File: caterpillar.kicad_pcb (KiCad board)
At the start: 4 copper layers, 18.3 x 20.3 mm, 33 parts, among them J1 Conn_ARM_JTAG_SWD_10, J2 SM02B-SRSS-TB_LF__SN_, J3 Castellated_2PTH_P1.27mm, J4 Castellated_2PTH_P1.27mm, M2 *, U1 STBB1-APUR, U2 ASM330LHHTR, U3 DRV8212P, U4 ADP2503ACPZ-3.3-R7, U6 max5419leta+T

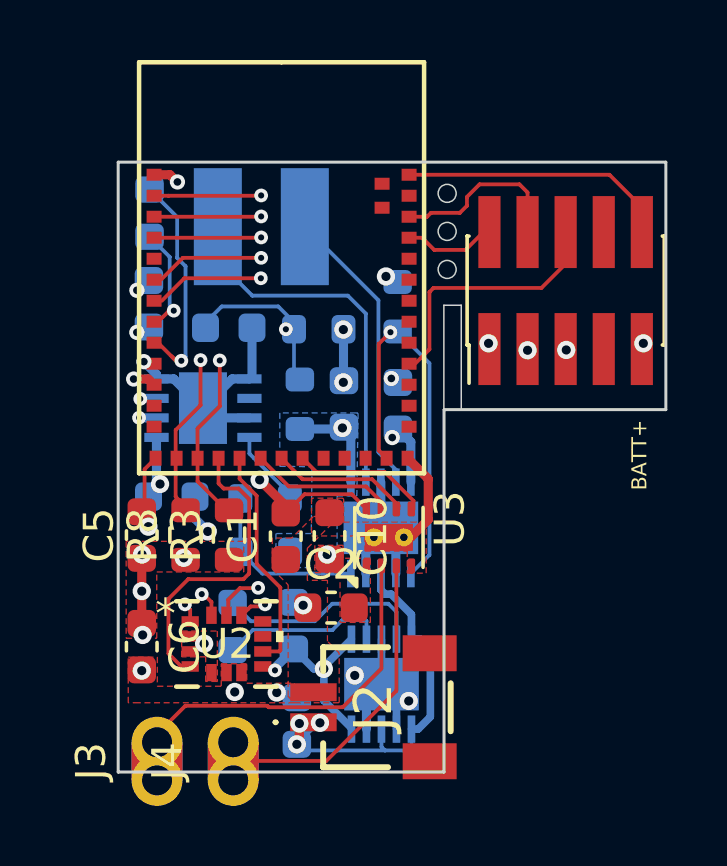
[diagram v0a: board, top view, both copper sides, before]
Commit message: all electrical issues fixed. Add as many vias as possible. connected nets on the same layer with polygon fills as much as possible. vias roughly realigned so looks much better
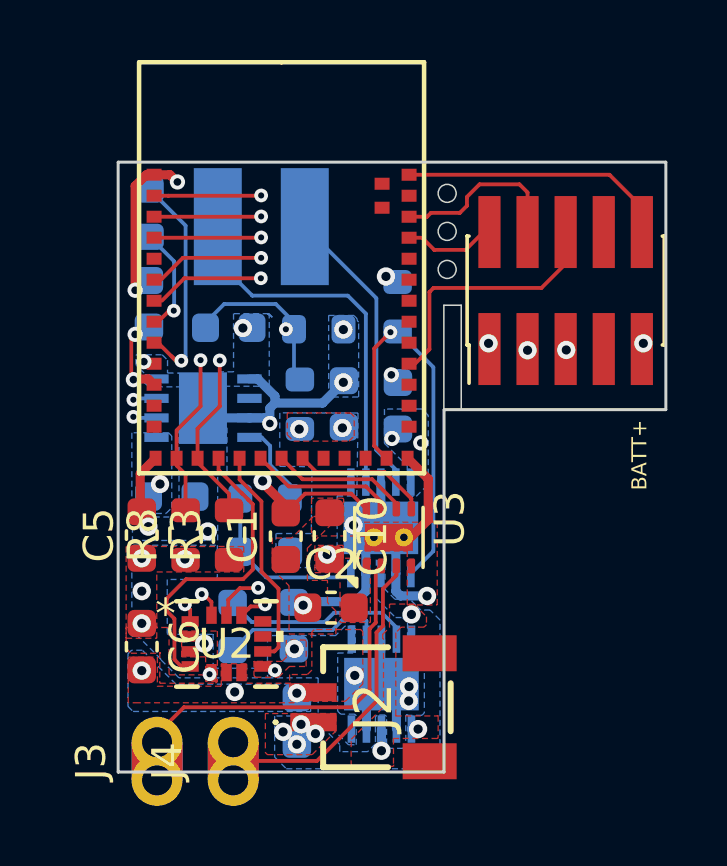
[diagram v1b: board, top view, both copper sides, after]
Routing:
- net +BATT: track 15.6 -> 1.89 mm, vias 4 -> 9
- net +3.3V: track 15.2 -> 7.11 mm, vias 12 -> 13
- net GND: track 26.8 -> 31.7 mm, vias 18 -> 23
- net VDC: track 3.42 -> 0.41 mm, vias 2 -> 3
- net /SCL: track 9.56 -> 10.5 mm
- net /CS: track 19.3 -> 20.3 mm
- net /SDA: track 8.97 -> 9.89 mm
- net /SCLK: track 18.7 -> 19.5 mm
- net /MISO: track 16.2 -> 16.7 mm
- net Net-(U4-SW1): track 6.98 -> 6.45 mm
- net /MOSI: track 16.9 -> 17.4 mm
- added copper zone on B.Cu, net +3.3V
- added copper zone on B.Cu, net +BATT
- added copper zone on F.Cu, net +BATT
- added copper zone on B.Cu, net GND

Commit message: thickened the power tracks of motor driver, added more vias for VDC output, moved VDC_sense away from the SW2
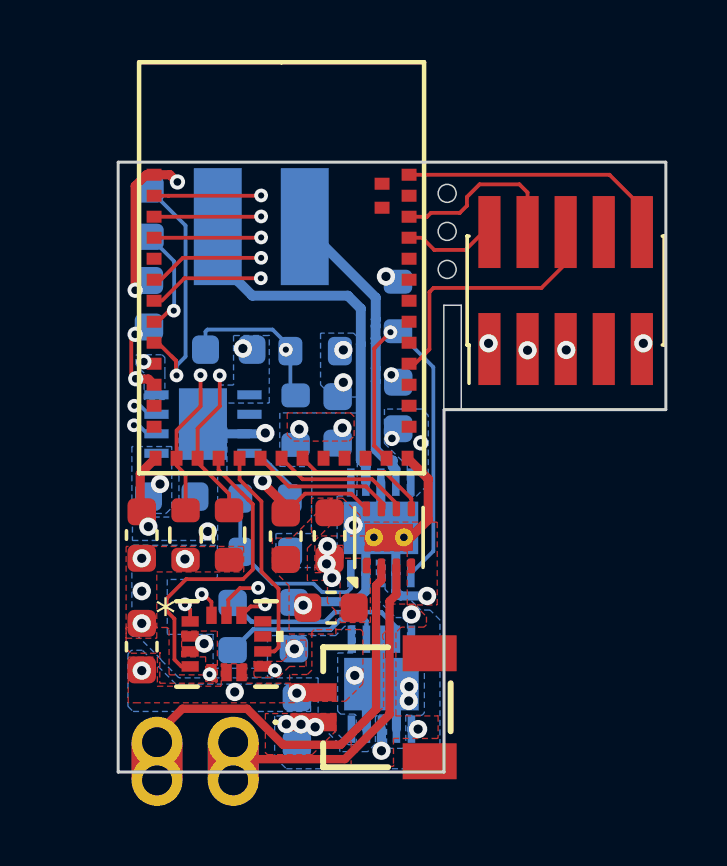
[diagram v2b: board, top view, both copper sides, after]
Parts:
- moved R5 0.74 mm to (116.6, 96.3)
- moved C13 0.73 mm to (113.7, 96.3)
- moved C9 0.57 mm to (117.3, 98.6)
- moved R6 0.55 mm to (116.0, 98.6)
- moved U6 0.53 mm to (112.9, 98.7)
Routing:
- net GND: track 31.7 -> 26.7 mm
- net /OUT1: track 12.0 -> 13.5 mm
- net Net-(M2-DCC): track 7.63 -> 8.53 mm
- net /OUT2: track 10.5 -> 11.3 mm
- net /FB: track 5.86 -> 6.56 mm
- net /SCL: track 10.5 -> 9.94 mm
- net /pot_H: track 2.83 -> 2.24 mm
- net /SDA: track 9.89 -> 9.37 mm
- net VDC: track 0.41 -> 0.08 mm, vias 3 -> 5
- net +BATT: track 1.89 -> 1.72 mm, vias 9 -> 8
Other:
- board text removed: "BATT+"

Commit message: pcb: shorten SPI runs inside the In2 GND plane by ~40%
Inner-layer signal routing reduced 65.4mm -> 45.2mm (CS 15.9->9.4,
SCLK 14.3->8.2, MOSI 12.9->8.6, MISO 12.5->8.9mm), shrinking the
slots cut through the GND plane. Remaining in-plane routing is a
recorded conscious-accept (slow SPI, short runs, board full on both
outer layers); to be validated at first article via IMU noise floor
with motor running + BLE RSSI A/B.
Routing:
- net /MISO: track 16.7 -> 13.7 mm
- net /MOSI: track 17.4 -> 15.0 mm

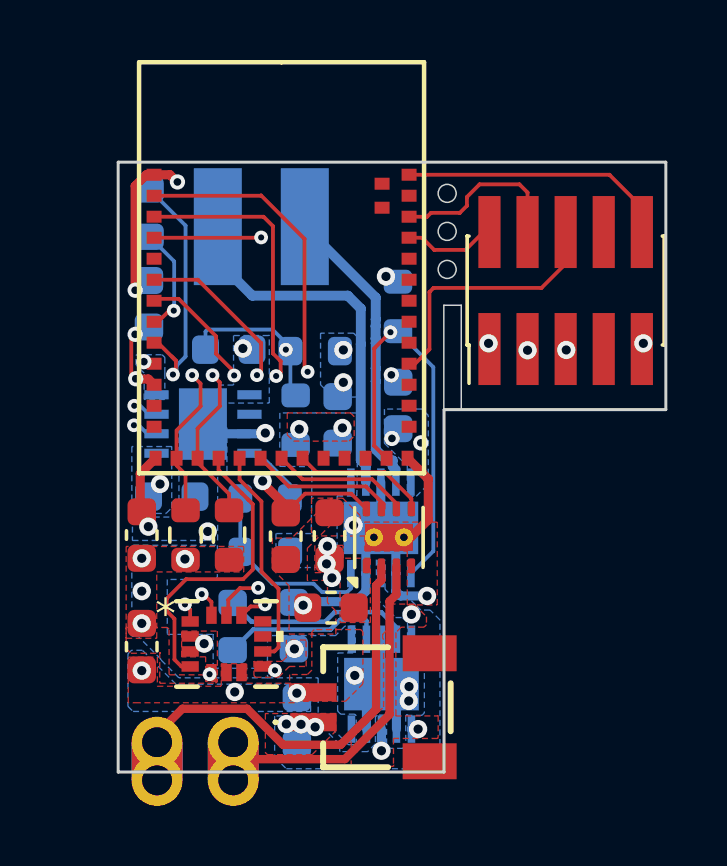
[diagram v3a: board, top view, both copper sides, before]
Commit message: pcb: fix via-in-pad and hole-spacing DFM findings (scripted, DRC-verified)
- deleted middle +BATT via of the triple at J2 (fixed both <0.25mm
  hole pairs there at once) plus its leftover stub
- U2 pad 5 (LGA, un-reworkable under package): 0.2mm via pulled out
  of the pad, reconnected with a 0.15mm stub
- VDC pair at C10: via repositioned within the same-net pad, all
  three VDC vias now >0.25mm hole-to-hole
- U4 EP: third thermal via deleted instead of relocated (no legal
  spot between OUT1/OUT2 and the J2 mounting pad; 2 vias ample for
  the light-load 3.3V converter)
- kept: J2 battery-pad vias (no legal landing site in that density;
  mitigate with flux/extra solder at assembly) and 0603/EP
  via-in-pad instances (accepted class; plugged-via fab option
  available if ever outsourced)

Final DRC: 0 shorts, 0 hole clearance, 0 hole-to-hole, 0 copper
clearance, 0 unconnected. Took 3 scripted rounds; rounds 1-2 created
shorts against OUT1/OUT2 caught by verification DRC and reverted.
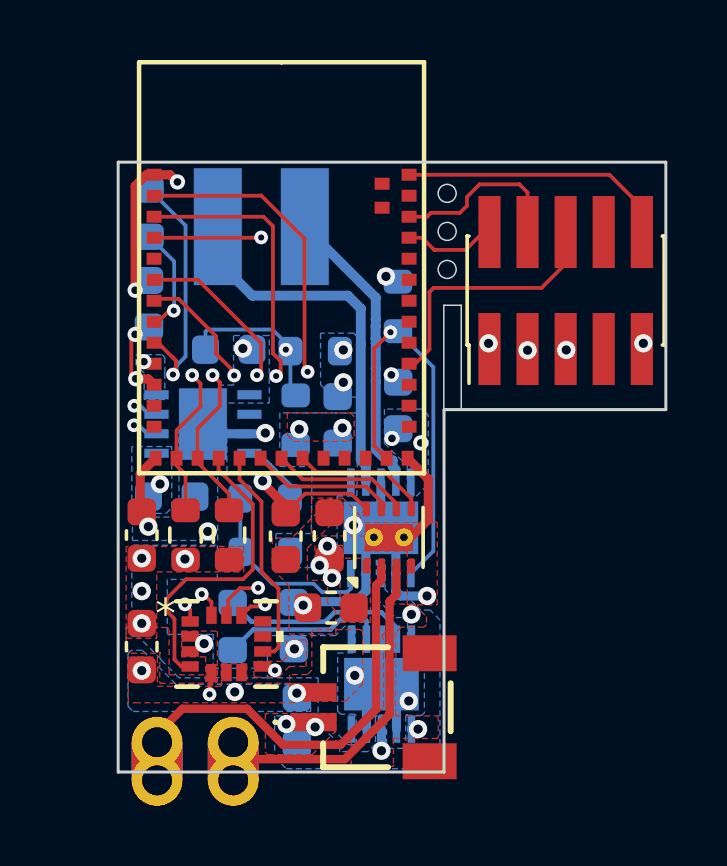
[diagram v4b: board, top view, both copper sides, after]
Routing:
- net +3.3V: track 6.98 -> 7.70 mm
- net +BATT: track 1.72 -> 1.64 mm, vias 8 -> 7
- net GND: vias 23 -> 22
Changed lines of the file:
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@@
+	)
+	(segment
+		(start 113.14 107.03)
+		(end 113.08 107.75)
+		(width 0.15)
+		(layer "F.Cu")
+		(net "+3.3V")
 	)
 	(segment
@@
 	)
 	(via
-		(at 113.08 107.08)
+		(at 113.08 107.75)
 		(size 0.4572)
 		(drill 0.2032)
@@
 	)
 	(via
-		(at 119.73 107.49)
-		(size 0.6096)
-		(drill 0.3048)
-		(layers "F.Cu" "B.Cu")
-		(net "GND")
-	)
-	(via
 		(at 114.94 99.04)
 		(size 0.6096)
@@
 	)
 	(via
-		(at 116.98 103.4)
+		(at 116.75 103.45)
 		(size 0.6096)
 		(drill 0.3048)
@@
 		(net "/OUT2")
 	)
-	(segment
-		(start 116.13 108.75)
-		(end 116.074756 108.805244)
-		(width 0.3048)
-		(layer "F.Cu")
-		(net "+BATT")
-	)
-	(via
-		(at 116.13 108.75)
-		(size 0.6096)
-		(drill 0.3048)
-		(layers "F.Cu" "B.Cu")
-		(net "+BATT")
-	)
-	(via
+	(via

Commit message: drc: edge clearance 0.2mm (PCBWay routed min) + by-design edge-copper rule
- min_copper_edge_clearance 0.254 -> 0.2mm: legitimizes M2 module pads
  (0.22mm) and L5 pads (0.20mm), both within PCBWay standard capability
- new dru rule 'edge_copper_by_design': edge_clearance min -1mm scoped
  to J3/J4 (castellations must cross the edge; clearance is negative,
  not zero) and J2 (accepted mounting-pad overhang)
- also: removed relocated U2.5 via + stub (owner edit); VDD_IO is fed
  by the F.Cu 3.3V pour + existing via 1mm away, GND pour stays whole

DRC: copper_edge_clearance 14 -> 0; all critical categories remain 0.
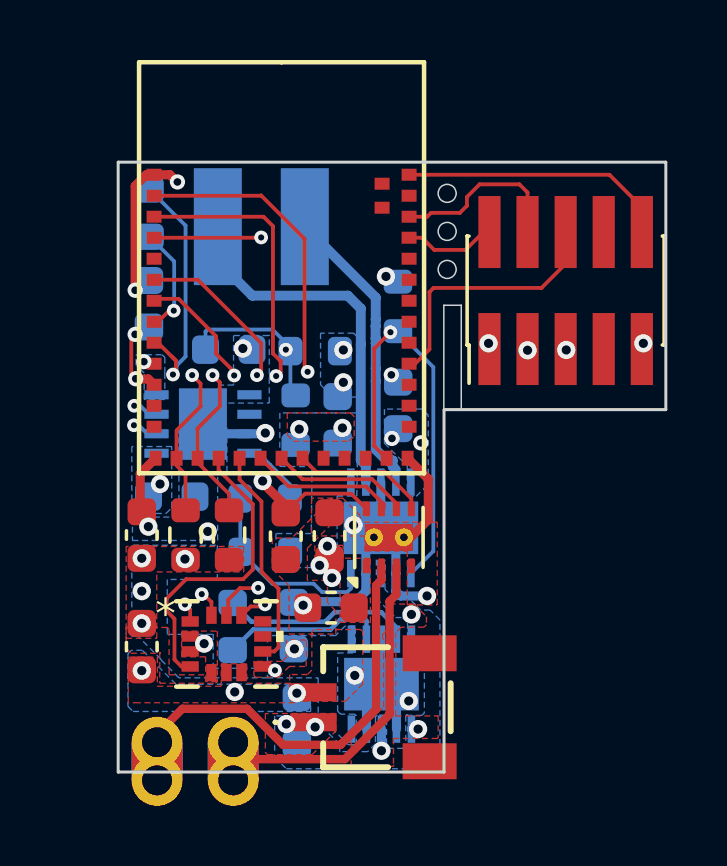
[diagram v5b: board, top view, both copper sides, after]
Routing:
- net +3.3V: track 7.70 -> 6.98 mm, vias 13 -> 12
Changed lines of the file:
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@@
-	)
-	(segment
-		(start 113.14 107.03)
-		(end 113.08 107.75)
-		(width 0.15)
-		(layer "F.Cu")
-		(net "+3.3V")
 	)
 	(segment
@@
 		(layers "F.Cu" "B.Cu")
 		(net "+3.3V")
-	)
-	(via
-		(at 113.08 107.75)
-		(size 0.4572)
-		(drill 0.2032)
-		(layers "F.Cu" "B.Cu")
-		(net "+3.3V")
